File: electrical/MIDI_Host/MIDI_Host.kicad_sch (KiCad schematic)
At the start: 45 parts, among them CN1 USB-CON-AF-LCP-Offset, J1 MC-107DM, J2 (NF), SW1 ST-0-102-C03-N003-RS, SW2 TC-1109DE-C-G, U11 BL1551B, U12 BL1551B, U14 SESRV05-4, U15 SESRV05-4, U16 BL1551B, U17 74HC165, U4 ESP32-S3-WROOM-1U, U8 BL1551B

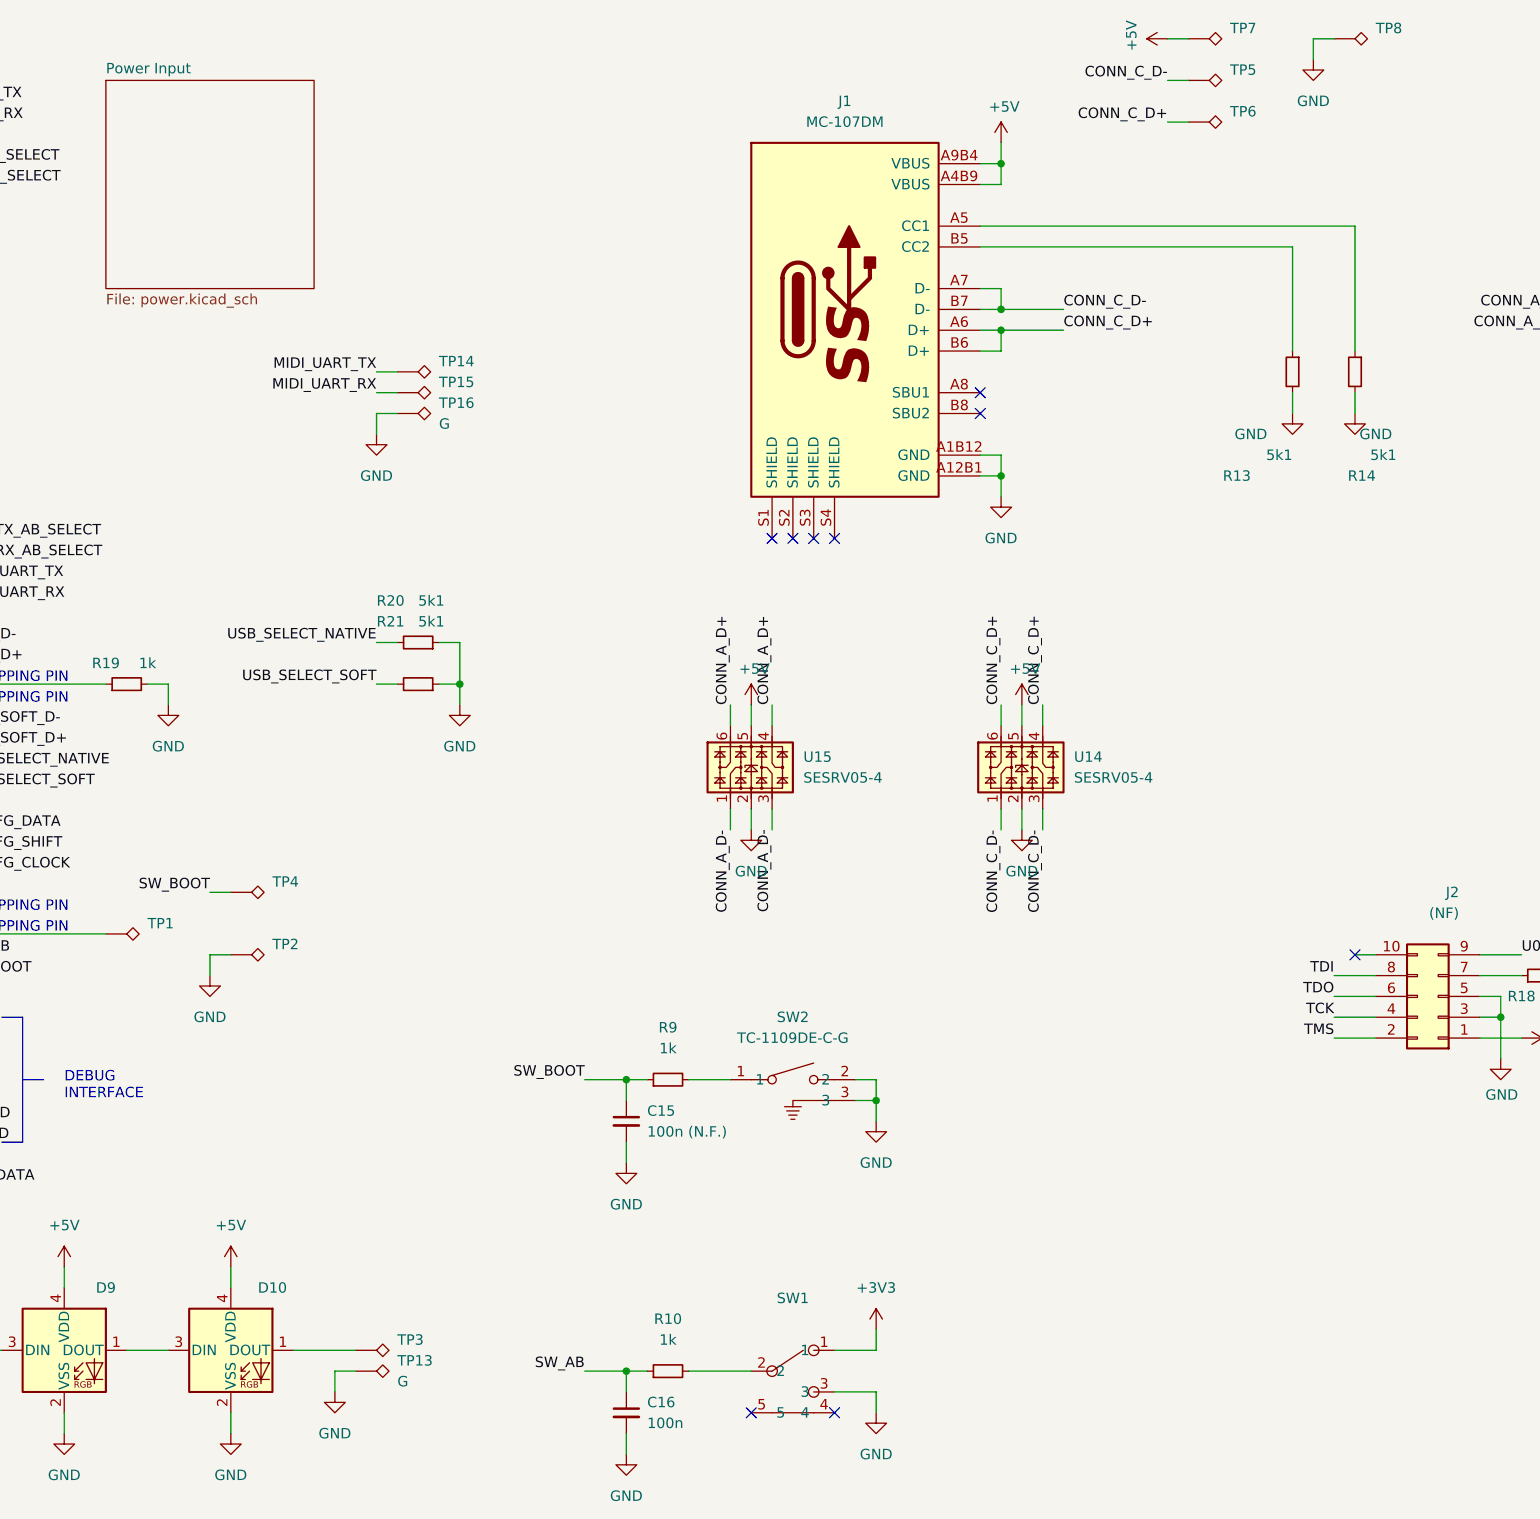
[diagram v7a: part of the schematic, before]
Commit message: SUKU capacitor footprint fixed,packup placement added
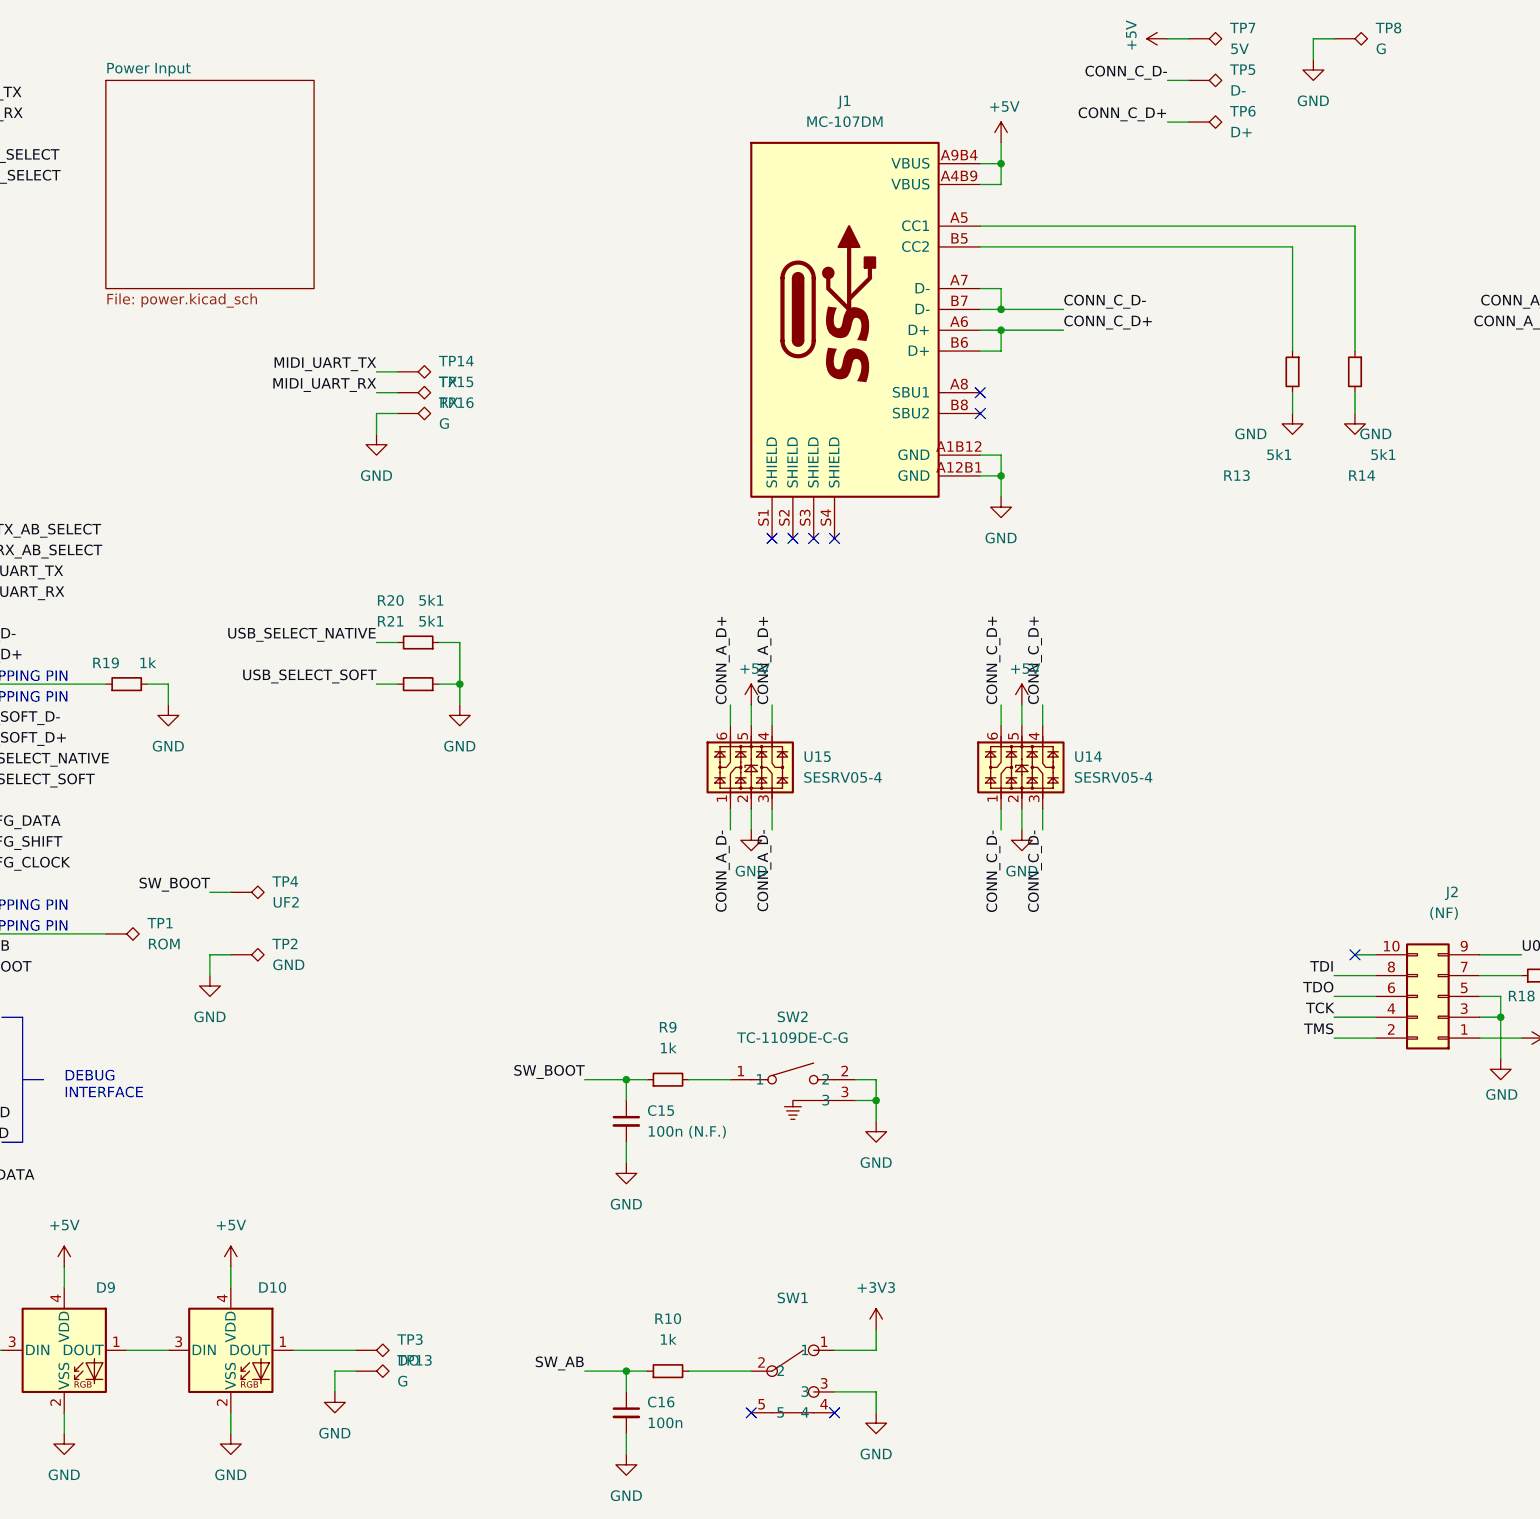
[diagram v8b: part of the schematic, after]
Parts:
- TP1: value (none) -> ROM; footprint (none) -> TestPoint:TestPoint_THTPad_D1.0mm_Drill0.5mm
- TP14: value (none) -> TX; footprint (none) -> TestPoint:TestPoint_THTPad_D1.0mm_Drill0.5mm
- TP15: value (none) -> RX; footprint (none) -> TestPoint:TestPoint_THTPad_D1.0mm_Drill0.5mm
- TP2: value (none) -> GND; footprint (none) -> TestPoint:TestPoint_THTPad_1.0x1.0mm_Drill0.5mm
- TP3: value (none) -> DO
- TP4: value (none) -> UF2
- TP5: value (none) -> D-
- TP6: value (none) -> D+
- TP7: value (none) -> 5V
- TP8: value (none) -> G
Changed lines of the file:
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@@
       (effects (font (size 1.27 1.27)) (justify left))
     )
-    (property "Value" "" (id 1) (at 218.44 19.0499 90)
+    (property "Value" "5V" (id 1) (at 218.44 19.0499 90)
       (effects (font (size 1.27 1.27)) (justify left))
     )
@@
       (effects (font (size 1.27 1.27)) (justify left))
     )
-    (property "Value" "" (id 1) (at 121.92 59.6899 90)
-      (effects (font (size 1.27 1.27)) (justify left))
-    )
-    (property "Footprint" "" (id 2) (at 116.84 63.5 0)
+    (property "Value" "TX" (id 1) (at 121.92 59.6899 90)
+      (effects (font (size 1.27 1.27)) (justify left))
+    )
+    (property "Footprint" "TestPoint:TestPoint_THTPad_D1.0mm_Drill0.5mm" (id 2) (at 116.84 63.5 0)
       (effects (font (size 1.27 1.27)) hide)
     )
@@
       (effects (font (size 1.27 1.27)) (justify left))
     )
-    (property "Value" "" (id 1) (at 86.36 128.2699 90)
-      (effects (font (size 1.27 1.27)) (justify left))
-    )
-    (property "Footprint" "" (id 2) (at 81.28 132.08 0)
+    (property "Value" "ROM" (id 1) (at 86.36 128.2699 90)
+      (effects (font (size 1.27 1.27)) (justify left))
+    )
+    (property "Footprint" "TestPoint:TestPoint_THTPad_D1.0mm_Drill0.5mm" (id 2) (at 81.28 132.08 0)
       (effects (font (size 1.27 1.27)) hide)
     )
@@
       (effects (font (size 1.27 1.27)) (justify left))
     )
-    (property "Value" "" (id 1) (at 218.44 29.2099 90)
+    (property "Value" "D+" (id 1) (at 218.44 29.2099 90)
       (effects (font (size 1.27 1.27)) (justify left))
     )
@@
       (effects (font (size 1.27 1.27)) (justify left))
     )
-    (property "Value" "" (id 1) (at 236.22 19.0499 90)
+    (property "Value" "G" (id 1) (at 236.22 19.0499 90)
       (effects (font (size 1.27 1.27)) (justify left))
     )
@@
       (effects (font (size 1.27 1.27)) (justify left))
     )
-    (property "Value" "" (id 1) (at 116.84 179.0699 90)
+    (property "Value" "DO" (id 1) (at 116.84 179.0699 90)
       (effects (font (size 1.27 1.27)) (justify left))
     )
@@
       (effects (font (size 1.27 1.27)) (justify left))
     )
-    (property "Value" "" (id 1) (at 101.6 130.8099 90)
-      (effects (font (size 1.27 1.27)) (justify left))
-    )
-    (property "Footprint" "" (id 2) (at 96.52 134.62 0)
+    (property "Value" "GND" (id 1) (at 101.6 130.8099 90)
+      (effects (font (size 1.27 1.27)) (justify left))
+    )
+    (property "Footprint" "TestPoint:TestPoint_THTPad_1.0x1.0mm_Drill0.5mm" (id 2) (at 96.52 134.62 0)
       (effects (font (size 1.27 1.27)) hide)
     )
@@
       (effects (font (size 1.27 1.27)) (justify left))
     )
-    (property "Value" "" (id 1) (at 101.6 123.1899 90)
+    (property "Value" "UF2" (id 1) (at 101.6 123.1899 90)
       (effects (font (size 1.27 1.27)) (justify left))
     )
@@
       (effects (font (size 1.27 1.27)) (justify left))
     )
-    (property "Value" "" (id 1) (at 121.92 62.2299 90)
-      (effects (font (size 1.27 1.27)) (justify left))
-    )
-    (property "Footprint" "" (id 2) (at 116.84 66.04 0)
+    (property "Value" "RX" (id 1) (at 121.92 62.2299 90)
+      (effects (font (size 1.27 1.27)) (justify left))
+    )
+    (property "Footprint" "TestPoint:TestPoint_THTPad_D1.0mm_Drill0.5mm" (id 2) (at 116.84 66.04 0)
       (effects (font (size 1.27 1.27)) hide)
     )
@@
       (effects (font (size 1.27 1.27)) (justify left))
     )
-    (property "Value" "" (id 1) (at 218.44 24.1299 90)
+    (property "Value" "D-" (id 1) (at 218.44 24.1299 90)
       (effects (font (size 1.27 1.27)) (justify left))
     )
@@
       (reference "#PWR0179") (unit 1) (value "GND") (footprint "")
     )
+    (path "/60c177f6-9f45-413f-893d-8d98077afbe8/cc741e4a-caf8-4fa0-a1eb-7a452183c306"
+      (reference "#PWR0180") (unit 1) (value "GND") (footprint "")
+    )
     (path "/78083a21-ffc6-4dac-bfdb-cbc4d5f4490c/f9f13c8c-5a65-4a40-baa1-7a6dcce8272f"
       (reference "Audio1") (unit 1) (value "PJ-320B") (footprint "suku_basics:AUDIO-SMD_PJ-320B")
@@
     )
     (path "/60c177f6-9f45-413f-893d-8d98077afbe8/82675026-40b9-4c1a-afef-c8916a0900a3"
-      (reference "C14") (unit 1) (value "CA45-C6R3K337T") (footprint "Capacitor_Tantalum_SMD:CP_EIA-6032-15_Kemet-U")
+      (reference "C14") (unit 1) (value "CA45-C6R3K337T") (footprint "suku_basics:CP_EIA-6032-15_Kemet-U")
     )
     (path "/a3d120f5-7006-4c4b-8261-16ea5805b5e7"
@@
       (reference "C18") (unit 1) (value "100n") (footprint "suku_basics:CAP_0805")
     )
+    (path "/60c177f6-9f45-413f-893d-8d98077afbe8/e90e04a4-2fa1-4750-af45-3d38f1d9d020"
+      (reference "C19") (unit 1) (value "(N.F.)") (footprint "suku_basics:CP_EIA-6032-15_Kemet-U")
+    )
     (path "/cc7fdda4-1f0b-4447-b8f5-2a7f9266383d"
